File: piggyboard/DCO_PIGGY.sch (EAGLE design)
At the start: 7 parts, among them P1 100KB, P2 100KB, P3 100KB

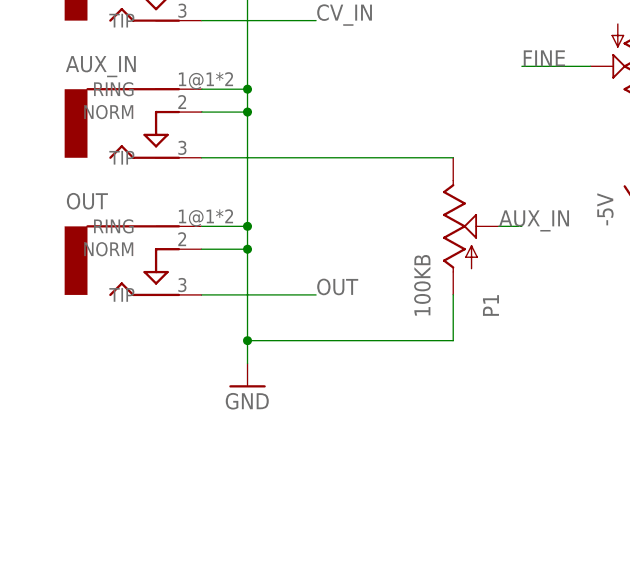
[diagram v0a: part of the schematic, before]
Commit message: fix for a messed up output jack on the piggy board
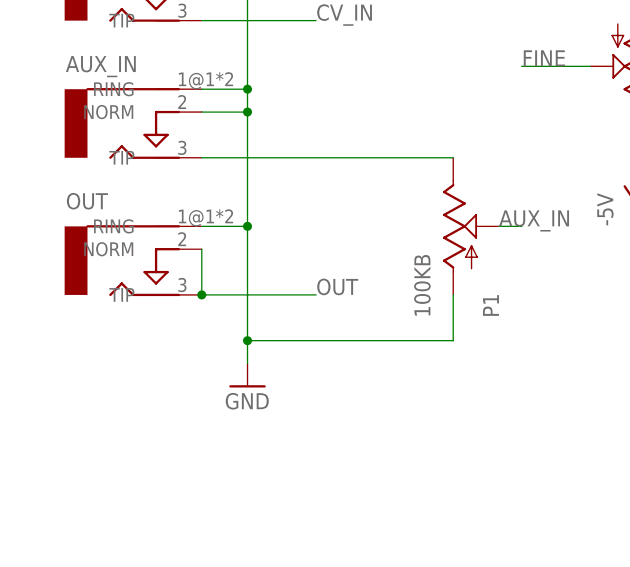
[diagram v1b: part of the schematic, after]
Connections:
- net GND: no longer OUT.NORM
- net OUT: now also OUT.NORM
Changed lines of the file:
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@@
 <?xml version="1.0" encoding="utf-8"?>
 <!DOCTYPE eagle SYSTEM "eagle.dtd">
-<eagle version="6.1">
+<eagle version="6.4">
 <drawing>
 <settings>
@@
 <setting verticaltext="up"/>
 </settings>
-<grid distance="0.1" unitdist="inch" unit="inch" style="lines" multiple="1" display="yes" altdistance="0.01" altunitdist="inch" altunit="inch"/>
+<grid distance="0.1" unitdist="inch" unit="inch" style="lines" multiple="1" display="no" altdistance="0.01" altunitdist="inch" altunit="inch"/>
 <layers>
 <layer number="1" name="Top" color="4" fill="1" visible="no" active="no"/>
@@
 <wire x1="25.4" y1="78.74" x2="25.4" y2="76.2" width="0.1524" layer="91"/>
 <wire x1="25.4" y1="76.2" x2="25.4" y2="63.5" width="0.1524" layer="91"/>
-<wire x1="25.4" y1="63.5" x2="25.4" y2="60.96" width="0.1524" layer="91"/>
-<wire x1="25.4" y1="60.96" x2="25.4" y2="50.8" width="0.1524" layer="91"/>
+<wire x1="25.4" y1="63.5" x2="25.4" y2="50.8" width="0.1524" layer="91"/>
 <wire x1="25.4" y1="50.8" x2="25.4" y2="48.26" width="0.1524" layer="91"/>
 <wire x1="20.32" y1="91.44" x2="25.4" y2="91.44" width="0.1524" layer="91"/>
@@
 <wire x1="20.32" y1="63.5" x2="25.4" y2="63.5" width="0.1524" layer="91"/>
 <junction x="25.4" y="63.5"/>
-<pinref part="OUT" gate="G$1" pin="NORM"/>
-<wire x1="20.32" y1="60.96" x2="25.4" y2="60.96" width="0.1524" layer="91"/>
-<junction x="25.4" y="60.96"/>
 <pinref part="GND1" gate="1" pin="GND"/>
 <pinref part="P1" gate="G$1" pin="A"/>
@@
 <wire x1="20.32" y1="55.88" x2="33.02" y2="55.88" width="0.1524" layer="91"/>
 <label x="33.02" y="55.88" size="1.778" layer="95"/>
+<pinref part="OUT" gate="G$1" pin="NORM"/>
+<wire x1="20.32" y1="60.96" x2="20.32" y2="55.88" width="0.1524" layer="91"/>
+<junction x="20.32" y="55.88"/>
 </segment>
 </net>

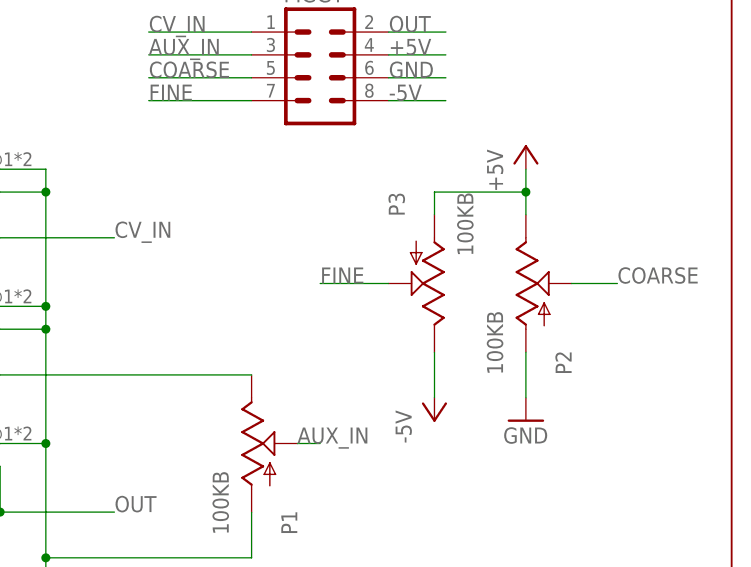
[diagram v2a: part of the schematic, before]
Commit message: Fix for design flaw - fine pitch control was attached backwards.
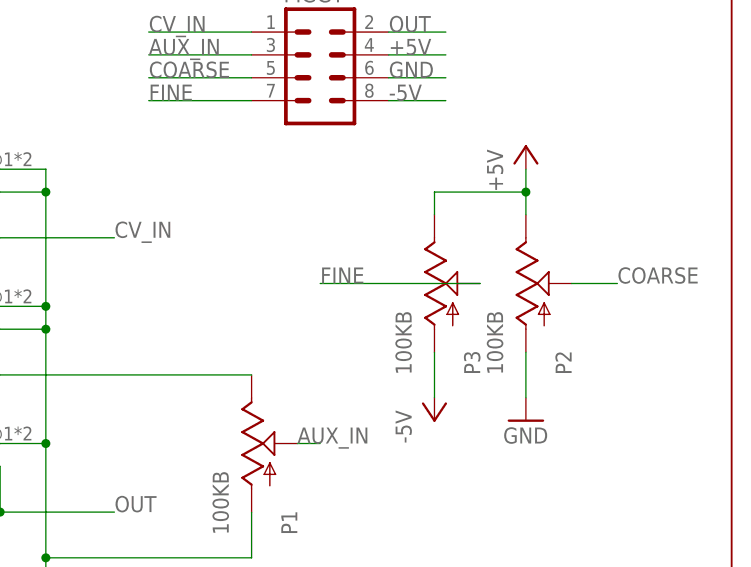
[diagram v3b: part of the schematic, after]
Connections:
- net +5V: now also P3.E; no longer P3.A
- net -5V: now also P3.A; no longer P3.E
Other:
- moved on the sheet: P3
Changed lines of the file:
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@@
 <instance part="GND2" gate="1" x="78.74" y="66.04"/>
 <instance part="P+1" gate="1" x="78.74" y="96.52"/>
-<instance part="P3" gate="G$1" x="68.58" y="81.28" rot="R180"/>
+<instance part="P3" gate="G$1" x="68.58" y="81.28"/>
 <instance part="P-1" gate="1" x="68.58" y="66.04"/>
 </instances>
@@
 <wire x1="78.74" y1="88.9" x2="78.74" y2="91.44" width="0.1524" layer="91"/>
 <pinref part="P+1" gate="1" pin="+5V"/>
-<pinref part="P3" gate="G$1" pin="A"/>
 <wire x1="78.74" y1="91.44" x2="78.74" y2="93.98" width="0.1524" layer="91"/>
-<wire x1="68.58" y1="88.9" x2="68.58" y2="91.44" width="0.1524" layer="91"/>
 <wire x1="68.58" y1="91.44" x2="78.74" y2="91.44" width="0.1524" layer="91"/>
 <junction x="78.74" y="91.44"/>
+<pinref part="P3" gate="G$1" pin="E"/>
+<wire x1="68.58" y1="91.44" x2="68.58" y2="88.9" width="0.1524" layer="91"/>
 </segment>
 </net>
@@
 </segment>
 <segment>
-<pinref part="P3" gate="G$1" pin="E"/>
+<pinref part="P3" gate="G$1" pin="A"/>
 <pinref part="P-1" gate="1" pin="-5V"/>
 <wire x1="68.58" y1="73.66" x2="68.58" y2="68.58" width="0.1524" layer="91"/>
@@
 <segment>
 <pinref part="P3" gate="G$1" pin="S"/>
-<wire x1="63.5" y1="81.28" x2="55.88" y2="81.28" width="0.1524" layer="91"/>
+<wire x1="73.66" y1="81.28" x2="55.88" y2="81.28" width="0.1524" layer="91"/>
 <label x="55.88" y="81.28" size="1.778" layer="95"/>
 </segment>
